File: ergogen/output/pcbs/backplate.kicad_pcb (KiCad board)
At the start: 2 copper layers, 134 x 92.5 mm, 0 parts

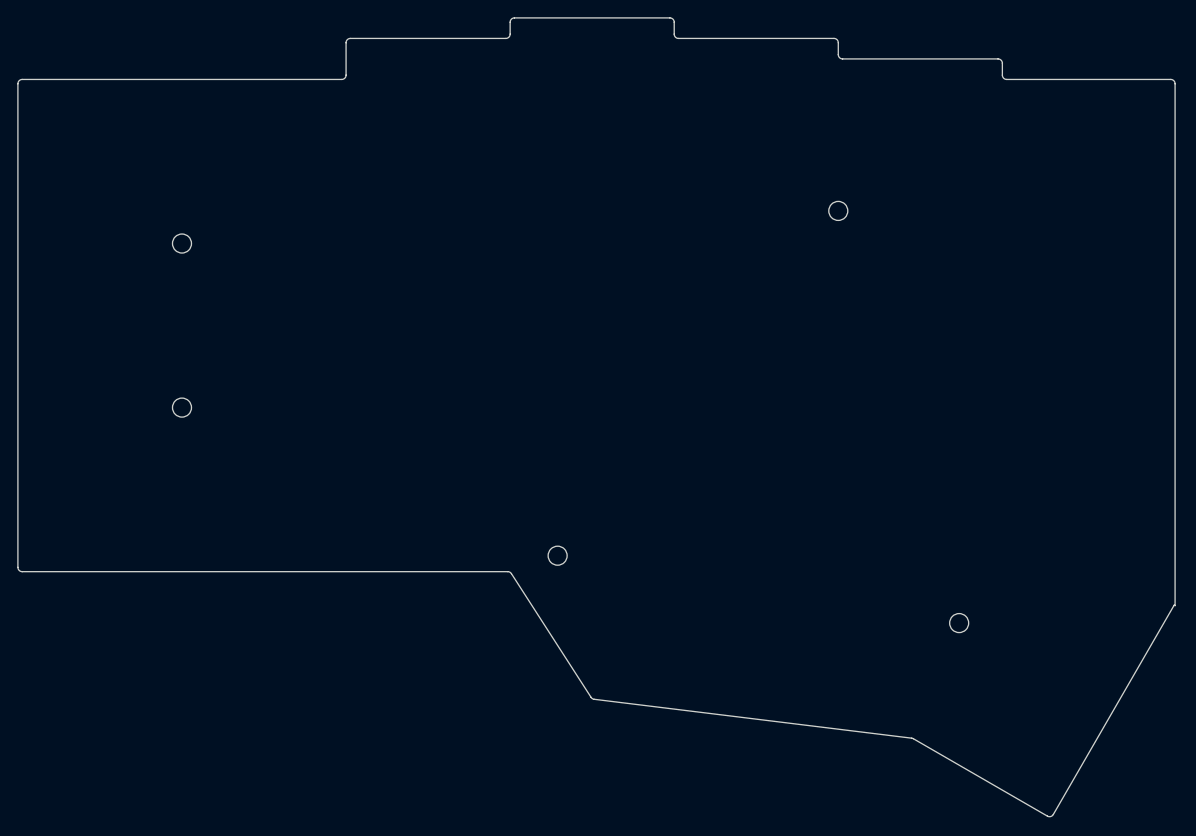
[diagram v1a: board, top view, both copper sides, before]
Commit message: Fix key positions to exactly match the corne
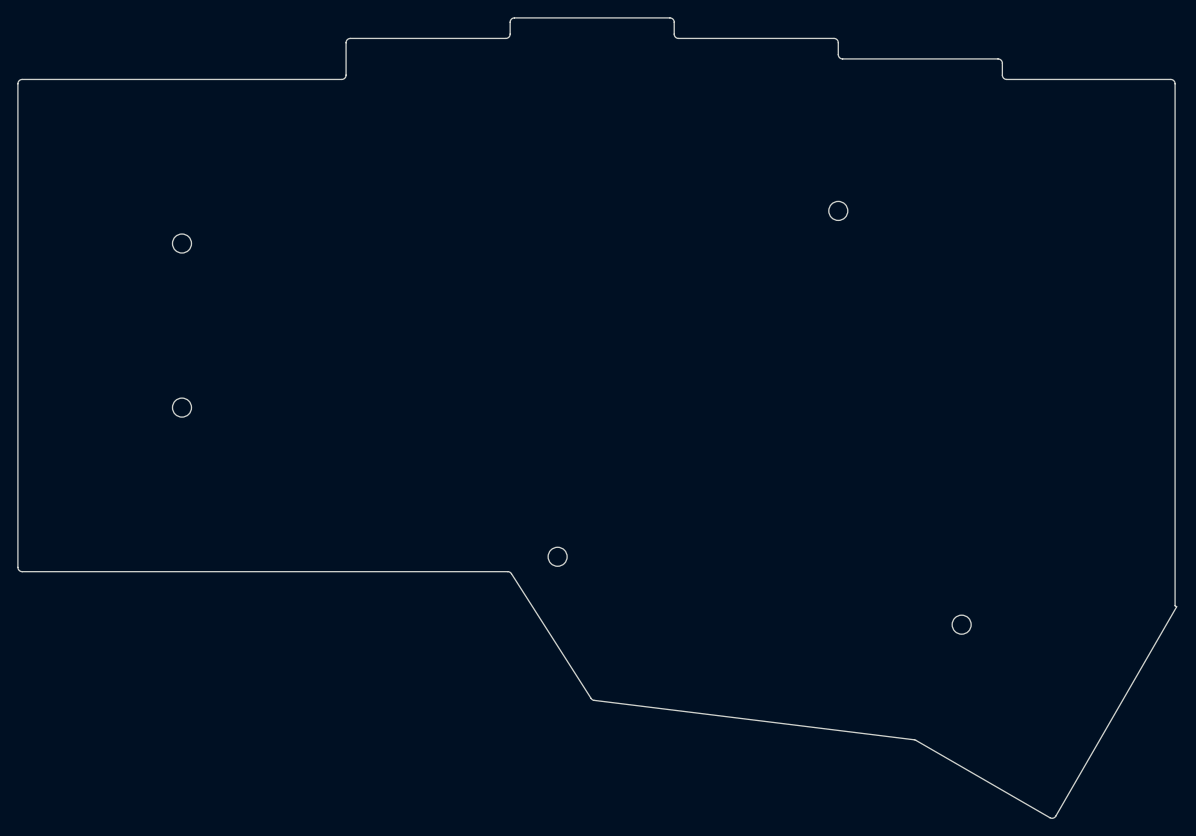
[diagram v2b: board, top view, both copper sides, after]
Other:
- board size 134 x 92.5 mm -> 134.2 x 92.7 mm
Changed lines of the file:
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@@
     (add_net "")
   )
-            (gr_line (start 91 109.5) (end 147.22730215593222 109.5) (angle 90) (layer Edge.Cuts) (width 0.15))
+            (gr_line (start 91 109.5) (end 147.226056907563 109.5) (angle 90) (layer Edge.Cuts) (width 0.15))
 (gr_line (start 90.5 109) (end 90.5 53) (angle 90) (layer Edge.Cuts) (width 0.15))
 (gr_line (start 91 52.5) (end 128 52.5) (angle 90) (layer Edge.Cuts) (width 0.15))
@@
 (gr_line (start 204.5 52) (end 204.5 50.625) (angle 90) (layer Edge.Cuts) (width 0.15))
 (gr_line (start 204 50.125) (end 186 50.125) (angle 90) (layer Edge.Cuts) (width 0.15))
-(gr_line (start 210.3979412988017 137.62313710032112) (end 224.39794129999996 113.3744258) (angle 90) (layer Edge.Cuts) (width 0.15))
-(gr_line (start 194.19299154809863 128.84455526290066) (end 209.71492859880163 137.80614980032107) (angle 90) (layer Edge.Cuts) (width 0.15))
-(gr_line (start 147.6476597559322 109.72926120000002) (end 156.8730776751543 124.05293639037114) (angle 90) (layer Edge.Cuts) (width 0.15))
-(gr_line (start 157.2326620183834 124.27849049566476) (end 194.00376480486958 128.78127505760708) (angle 90) (layer Edge.Cuts) (width 0.15))
-(gr_line (start 224.5 113.43334944776565) (end 224.5 53) (angle 90) (layer Edge.Cuts) (width 0.15))
+(gr_line (start 210.68768509880175 137.80950690032108) (end 224.6876851 113.56079560000002) (angle 90) (layer Edge.Cuts) (width 0.15))
+(gr_line (start 224.5 113.45243558639906) (end 224.6876851 113.56079560000002) (angle 90) (layer Edge.Cuts) (width 0.15))
+(gr_line (start 194.4825814717975 129.0308362223767) (end 210.00467239880174 137.99251960032112) (angle 90) (layer Edge.Cuts) (width 0.15))
+(gr_line (start 147.6474496930774 109.73087517731855) (end 156.87331650010177 124.17664030936987) (angle 90) (layer Edge.Cuts) (width 0.15))
+(gr_line (start 157.23359753636308 124.40376678062299) (end 194.2936932210506 128.9675976284421) (angle 90) (layer Edge.Cuts) (width 0.15))
+(gr_line (start 224.5 113.45243558639906) (end 224.5 53) (angle 90) (layer Edge.Cuts) (width 0.15))
 (gr_line (start 224 52.5) (end 205 52.5) (angle 90) (layer Edge.Cuts) (width 0.15))
-(gr_line (start 224.5 113.43334944776565) (end 224.39794129999996 113.3744258) (angle 90) (layer Edge.Cuts) (width 0.15))
-(gr_arc (start 147.22730215593222 110) (end 147.6476597559322 109.7292612) (angle -57.2157184809877) (layer Edge.Cuts) (width 0.15))
-(gr_arc (start 157.2934352751543 123.78219759037117) (end 156.87307767515432 124.05293639037117) (angle -50.23435431888237) (layer Edge.Cuts) (width 0.15))
-(gr_arc (start 193.94299154809863 129.27756796290063) (end 194.19299154809863 128.84455526290063) (angle -23.01863594630671) (layer Edge.Cuts) (width 0.15))
-(gr_arc (start 209.96492859880166 137.37313710032106) (end 209.71492859880166 137.80614980032107) (angle -89.99999999999889) (layer Edge.Cuts) (width 0.15))
+(gr_arc (start 147.226056907563 110) (end 147.647449607563 109.7308752) (angle -57.4354397170889) (layer Edge.Cuts) (width 0.15))
+(gr_arc (start 157.2947092856161 123.90751548668835) (end 156.8733165856161 124.17664028668835) (angle -50.414995185869486) (layer Edge.Cuts) (width 0.15))
+(gr_arc (start 194.23258147179752 129.4638489223767) (end 194.48258147179752 129.0308362223767) (angle -22.979555577197353) (layer Edge.Cuts) (width 0.15))
+(gr_arc (start 210.25467239880174 137.5595069003211) (end 210.00467239880174 137.99251960032112) (angle -90.00000000000279) (layer Edge.Cuts) (width 0.15))
 (gr_arc (start 224 53) (end 224.5 53) (angle -90) (layer Edge.Cuts) (width 0.15))
 (gr_arc (start 205 52) (end 204.5 52) (angle -90) (layer Edge.Cuts) (width 0.15))
@@
 (gr_circle (center 109.5 90.5) (end 110.6 90.5) (layer Edge.Cuts) (width 0.15))
 (gr_circle (center 185.5 67.725) (end 186.6 67.725) (layer Edge.Cuts) (width 0.15))
-(gr_circle (center 153 107.65) (end 154.1 107.65) (layer Edge.Cuts) (width 0.15))
-(gr_circle (center 199.49776989999998 115.4527878) (end 200.59776989999997 115.4527878) (layer Edge.Cuts) (width 0.15))
+(gr_circle (center 153 107.775) (end 154.1 107.775) (layer Edge.Cuts) (width 0.15))
+(gr_circle (center 199.7875137 115.6391576) (end 200.8875137 115.6391576) (layer Edge.Cuts) (width 0.15))
 )

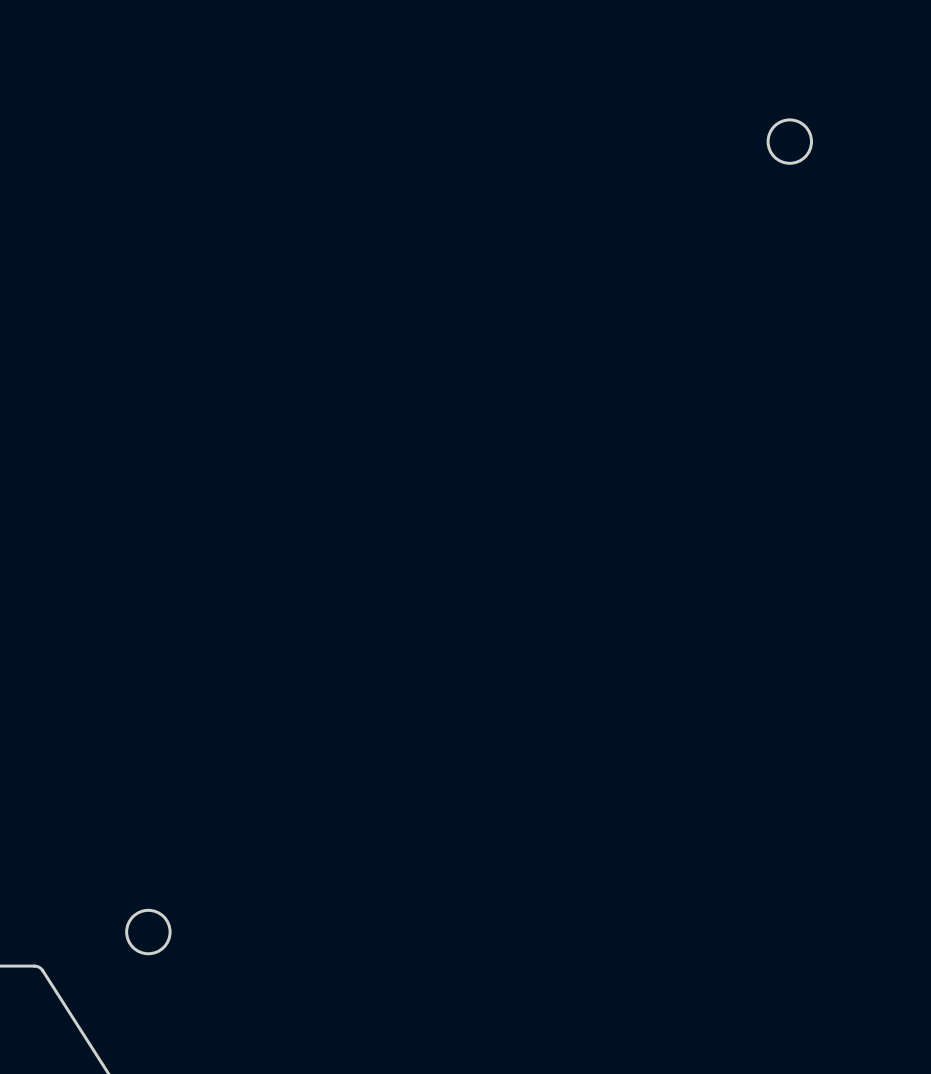
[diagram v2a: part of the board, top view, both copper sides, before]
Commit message: Fix MCU cover mounting holes position
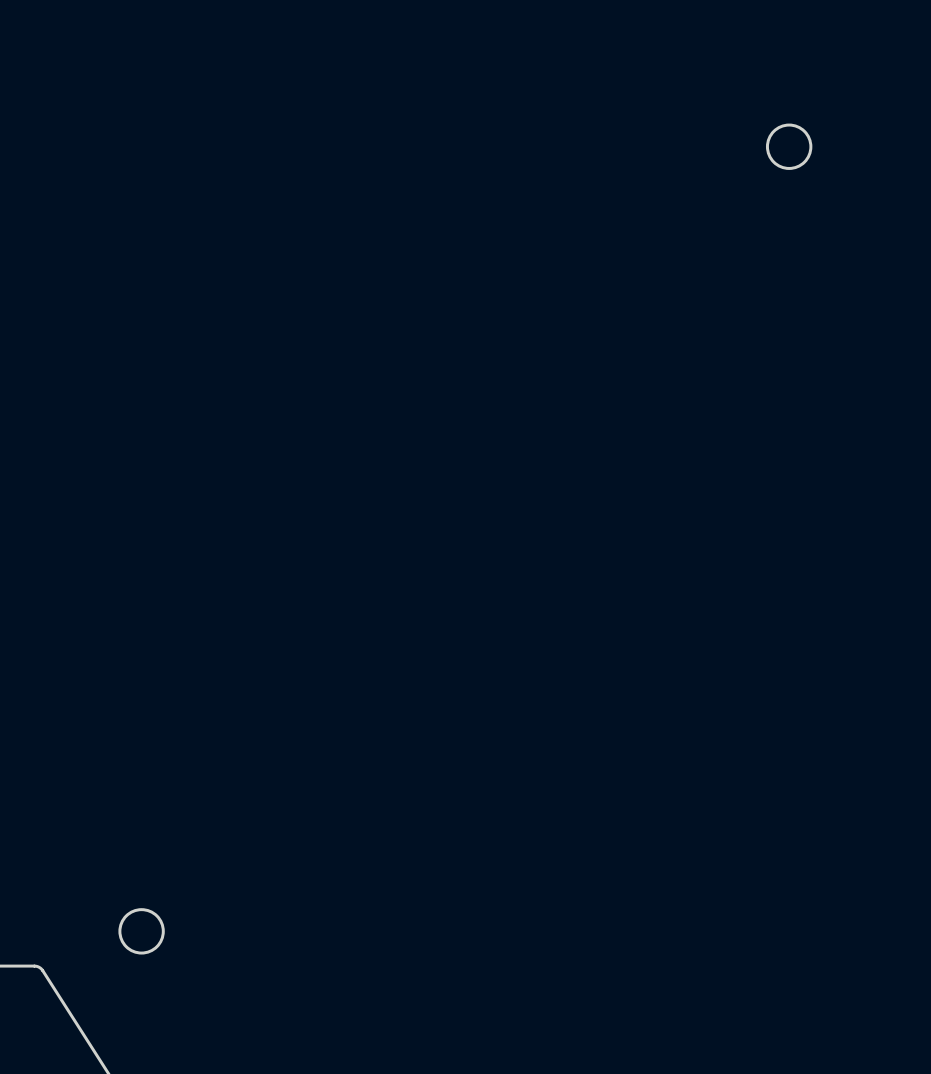
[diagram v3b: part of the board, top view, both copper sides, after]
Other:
- outline, holes or cut-outs redrawn
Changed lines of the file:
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@@
 (gr_circle (center 109.5 71.5) (end 110.6 71.5) (layer Edge.Cuts) (width 0.15))
 (gr_circle (center 109.5 90.5) (end 110.6 90.5) (layer Edge.Cuts) (width 0.15))
-(gr_circle (center 185.5 67.725) (end 186.6 67.725) (layer Edge.Cuts) (width 0.15))
-(gr_circle (center 153 107.775) (end 154.1 107.775) (layer Edge.Cuts) (width 0.15))
+(gr_circle (center 185.468 67.986) (end 186.56799999999998 67.986) (layer Edge.Cuts) (width 0.15))
+(gr_circle (center 152.657 107.74) (end 153.757 107.74) (layer Edge.Cuts) (width 0.15))
 (gr_circle (center 199.7875137 115.6391576) (end 200.8875137 115.6391576) (layer Edge.Cuts) (width 0.15))
 )

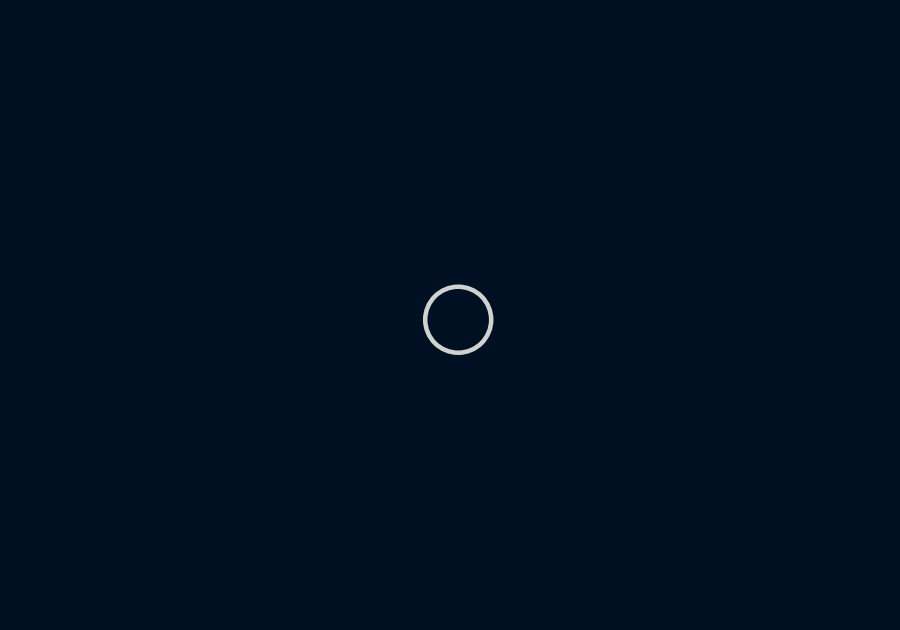
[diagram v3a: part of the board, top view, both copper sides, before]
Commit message: Fix inner underglow LED position
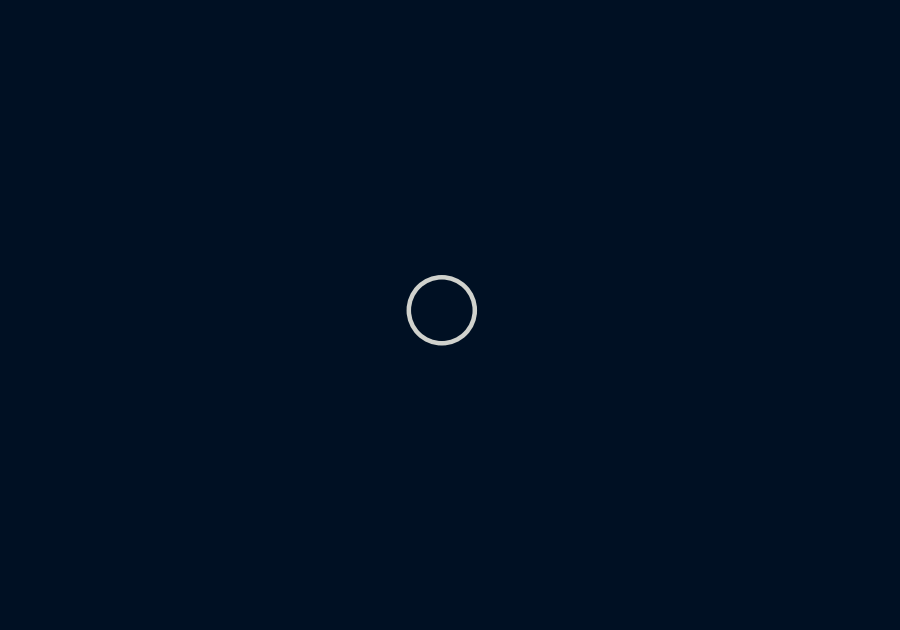
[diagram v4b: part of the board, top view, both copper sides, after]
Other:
- outline, holes or cut-outs redrawn
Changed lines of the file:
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@@
 (gr_circle (center 185.468 67.986) (end 186.56799999999998 67.986) (layer Edge.Cuts) (width 0.15))
 (gr_circle (center 152.657 107.74) (end 153.757 107.74) (layer Edge.Cuts) (width 0.15))
-(gr_circle (center 199.7875137 115.6391576) (end 200.8875137 115.6391576) (layer Edge.Cuts) (width 0.15))
+(gr_circle (center 199.2410516 115.3236576) (end 200.3410516 115.3236576) (layer Edge.Cuts) (width 0.15))
 )
